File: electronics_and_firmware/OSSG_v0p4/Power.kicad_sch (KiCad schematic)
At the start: 37 parts, among them J2 USB_B_Micro, Q3 PMZ290UNE2YL, Q4 EMF20B02V, SW2 Power, U4 XC61CC3002MR, U5 MP2615CGQ-Z, U6 H7650-50PR, U7 NCP167BMX330TBG

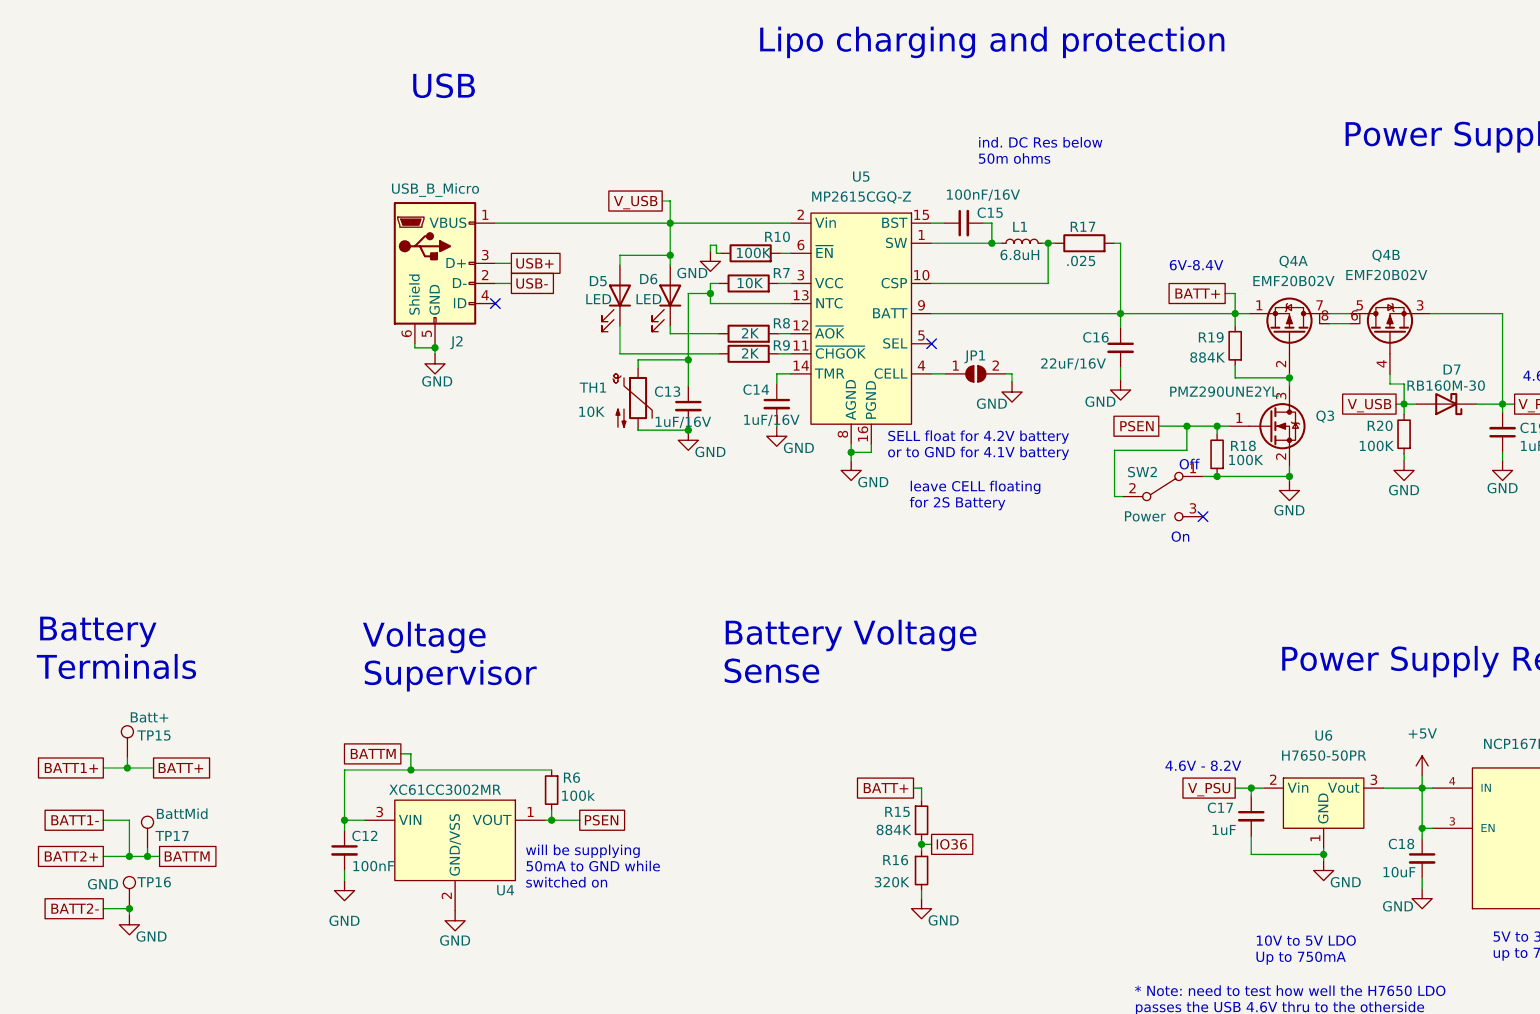
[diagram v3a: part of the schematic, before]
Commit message: adding in last update for the 2S branch design
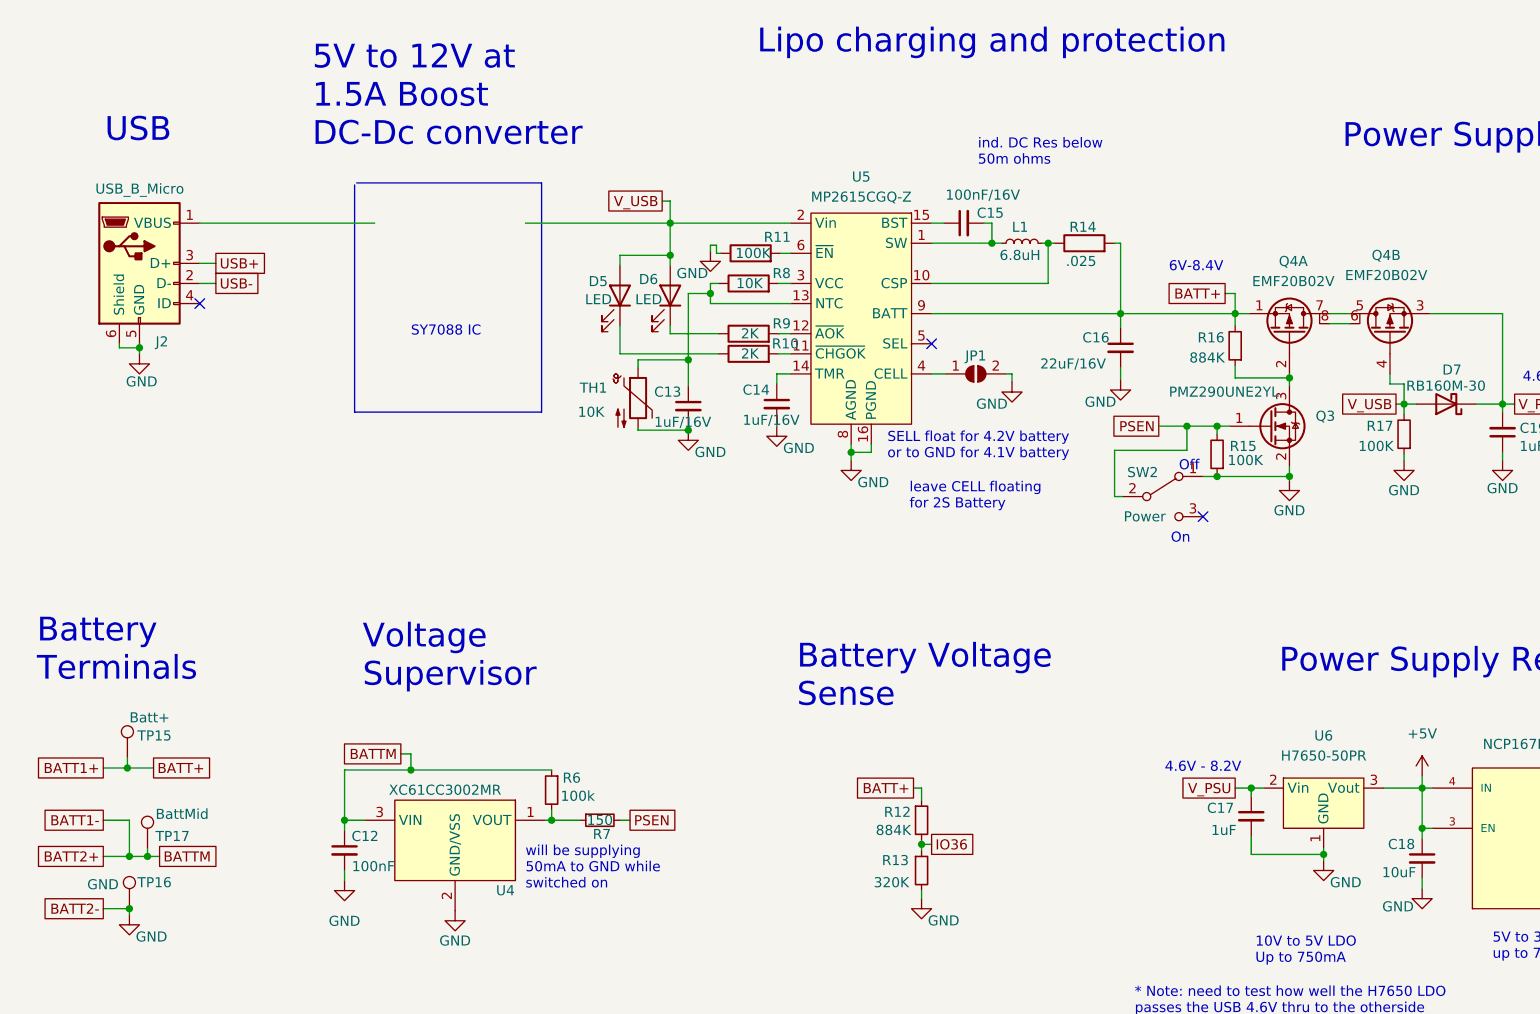
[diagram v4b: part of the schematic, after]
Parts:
- added R7: 150, Resistor_SMD:R_0402_1005Metric, symbol Device:R_Small
- renumbered R9 to R10, R10 to R11, R15 to R12, R16 to R13, R17 to R14, R18 to R15, R19 to R16, R20 to R17, R7 to R8, R8 to R9
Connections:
- net PSEN: now also R7.2; no longer R6.2, U4.1 (VOUT)
- net V_USB: no longer J2.1 (VBUS)
- new net: R6.2, R7.1, U4.1 (VOUT)
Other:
- note added: "5V to 12V at 1.5A Boost DC-Dc converter"
- note added: "SY7088 IC"
- title: (none) -> Team OpenSource Smartglasses
- moved on the sheet: J2
